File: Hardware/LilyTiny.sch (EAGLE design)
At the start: 13 parts, among them U1 ATTINY85

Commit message: Moved components to 0603 package size
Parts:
- C1: device SparkFun:CAP0402-CAP -> SparkFun:CAP0603-CAP
- R1: device SparkFun:RESISTOR0402-RES -> SparkFun:RESISTOR0603-RES
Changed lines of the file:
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@@
 <?xml version="1.0" encoding="utf-8"?>
 <!DOCTYPE eagle SYSTEM "eagle.dtd">
-<eagle version="6.1">
+<eagle version="6.4">
 <drawing>
 <settings>
@@
 <grid distance="0.1" unitdist="inch" unit="inch" style="lines" multiple="1" display="no" altdistance="0.01" altunitdist="inch" altunit="inch"/>
 <layers>
-<layer number="1" name="Top" color="4" fill="1" visible="no" active="no"/>
-<layer number="2" name="Route2" color="1" fill="3" visible="no" active="no"/>
-<layer number="3" name="Route3" color="4" fill="3" visible="no" active="no"/>
-<layer number="4" name="Route4" color="1" fill="4" visible="no" active="no"/>
-<layer number="5" name="Route5" color="4" fill="4" visible="no" active="no"/>
-<layer number="6" name="Route6" color="1" fill="8" visible="no" active="no"/>
-<layer number="7" name="Route7" color="4" fill="8" visible="no" active="no"/>
-<layer number="8" name="Route8" color="1" fill="2" visible="no" active="no"/>
-<layer number="9" name="Route9" color="4" fill="2" visible="no" active="no"/>
-<layer number="10" name="Route10" color="1" fill="7" visible="no" active="no"/>
-<layer number="11" name="Route11" color="4" fill="7" visible="no" active="no"/>
-<layer number="12" name="Route12" color="1" fill="5" visible="no" active="no"/>
-<layer number="13" name="Route13" color="4" fill="5" visible="no" active="no"/>
-<layer number="14" name="Route14" color="1" fill="6" visible="no" active="no"/>
-<layer number="15" name="Route15" color="4" fill="6" visible="no" active="no"/>
-<layer number="16" name="Bottom" color="1" fill="1" visible="no" active="no"/>
-<layer number="17" name="Pads" color="2" fill="1" visible="no" active="no"/>
-<layer number="18" name="Vias" color="2" fill="1" visible="no" active="no"/>
-<layer number="19" name="Unrouted" color="6" fill="1" visible="no" active="no"/>
-<layer number="20" name="Dimension" color="7" fill="1" visible="no" active="no"/>
-<layer number="21" name="tPlace" color="16" fill="1" visible="no" active="no"/>
-<layer number="22" name="bPlace" color="14" fill="1" visible="no" active="no"/>
-<layer number="23" name="tOrigins" color="15" fill="1" visible="no" active="no"/>
-<layer number="24" name="bOrigins" color="15" fill="1" visible="no" active="no"/>
-<layer number="25" name="tNames" color="7" fill="1" visible="no" active="no"/>
-<layer number="26" name="bNames" color="7" fill="1" visible="no" active="no"/>
-<layer number="27" name="tValues" color="7" fill="1" visible="no" active="no"/>
-<layer number="28" name="bValues" color="7" fill="1" visible="no" active="no"/>
+<layer number="1" name="Top" color="4" fill="1" visible="yes" active="no"/>
+<layer number="2" name="Route2" color="1" fill="3" visible="yes" active="no"/>
+<layer number="3" name="Route3" color="4" fill="3" visible="yes" active="no"/>
+<layer number="4" name="Route4" color="1" fill="4" visible="yes" active="no"/>
+<layer number="5" name="Route5" color="4" fill="4" visible="yes" active="no"/>
+<layer number="6" name="Route6" color="1" fill="8" visible="yes" active="no"/>
+<layer number="7" name="Route7" color="4" fill="8" visible="yes" active="no"/>
+<layer number="8" name="Route8" color="1" fill="2" visible="yes" active="no"/>
+<layer number="9" name="Route9" color="4" fill="2" visible="yes" active="no"/>
+<layer number="10" name="Route10" color="1" fill="7" visible="yes" active="no"/>
+<layer number="11" name="Route11" color="4" fill="7" visible="yes" active="no"/>
+<layer number="12" name="Route12" color="1" fill="5" visible="yes" active="no"/>
+<layer number="13" name="Route13" color="4" fill="5" visible="yes" active="no"/>
+<layer number="14" name="Route14" color="1" fill="6" visible="yes" active="no"/>
+<layer number="15" name="Route15" color="4" fill="6" visible="yes" active="no"/>
+<layer number="16" name="Bottom" color="1" fill="1" visible="yes" active="no"/>
+<layer number="17" name="Pads" color="2" fill="1" visible="yes" active="no"/>
+<layer number="18" name="Vias" color="2" fill="1" visible="yes" active="no"/>
+<layer number="19" name="Unrouted" color="6" fill="1" visible="yes" active="no"/>
+<layer number="20" name="Dimension" color="6" fill="1" visible="yes" active="no"/>
+<layer number="21" name="tPlace" color="16" fill="1" visible="yes" active="no"/>
+<layer number="22" name="bPlace" color="14" fill="1" visible="yes" active="no"/>
+<layer number="23" name="tOrigins" color="15" fill="1" visible="yes" active="no"/>
+<layer number="24" name="bOrigins" color="15" fill="1" visible="yes" active="no"/>
+<layer number="25" name="tNames" color="7" fill="1" visible="yes" active="no"/>
+<layer number="26" name="bNames" color="7" fill="1" visible="yes" active="no"/>
+<layer number="27" name="tValues" color="7" fill="1" visible="yes" active="no"/>
+<layer number="28" name="bValues" color="7" fill="1" visible="yes" active="no"/>
 <layer number="29" name="tStop" color="7" fill="3" visible="no" active="no"/>
 <layer number="30" name="bStop" color="7" fill="6" visible="no" active="no"/>
-<layer number="31" name="tCream" color="11" fill="4" visible="no" active="no"/>
+<layer number="31" name="tCream" color="7" fill="4" visible="no" active="no"/>
 <layer number="32" name="bCream" color="7" fill="5" visible="no" active="no"/>
 <layer number="33" name="tFinish" color="6" fill="3" visible="no" active="no"/>
@@
 <layer number="35" name="tGlue" color="7" fill="4" visible="no" active="no"/>
 <layer number="36" name="bGlue" color="7" fill="5" visible="no" active="no"/>
-<layer number="37" name="tTest" color="7" fill="1" visible="no" active="no"/>
-<layer number="38" name="bTest" color="7" fill="1" visible="no" active="no"/>
+<layer number="37" name="tTest" color="7" fill="1" visible="yes" active="no"/>
+<layer number="38" name="bTest" color="7" fill="1" visible="yes" active="no"/>
 <layer number="39" name="tKeepout" color="4" fill="11" visible="no" active="no"/>
 <layer number="40" name="bKeepout" color="1" fill="11" visible="no" active="no"/>
@@
 <layer number="44" name="Drills" color="7" fill="1" visible="no" active="no"/>
 <layer number="45" name="Holes" color="7" fill="1" visible="no" active="no"/>
-<layer number="46" name="Milling" color="3" fill="1" visible="no" active="no"/>
-<layer number="47" name="Measures" color="7" fill="1" visible="no" active="no"/>
-<layer number="48" name="Document" color="7" fill="1" visible="no" active="no"/>
-<layer number="49" name="Reference" color="13" fill="1" visible="no" active="no"/>
-<layer number="50" name="dxf" color="7" fill="1" visible="no" active="no"/>
-<layer number="51" name="tDocu" color="14" fill="1" visible="no" active="no"/>
-<layer number="52" name="bDocu" color="7" fill="1" visible="no" active="no"/>
-<layer number="53" name="tGND_GNDA" color="7" fill="9" visible="no" active="no"/>
-<layer number="54" name="bGND_GNDA" color="1" fill="9" visible="no" active="no"/>
-<layer number="56" name="wert" color="7" fill="1" visible="no" active="no"/>
+<layer number="46" name="Milling" color="3" fill="1" visible="yes" active="no"/>
+<layer number="47" name="Measures" color="7" fill="1" visible="yes" active="no"/>
+<layer number="48" name="Document" color="7" fill="1" visible="yes" active="no"/>
+<layer number="49" name="Reference" color="7" fill="1" visible="yes" active="no"/>
+<layer number="50" name="dxf" color="7" fill="1" visible="yes" active="no"/>
+<layer number="51" name="tDocu" color="6" fill="1" visible="yes" active="no"/>
+<layer number="52" name="bDocu" color="7" fill="1" visible="yes" active="no"/>
+<layer number="53" name="tGND_GNDA" color="7" fill="9" visible="yes" active="no"/>
+<layer number="54" name="bGND_GNDA" color="1" fill="9" visible="yes" active="no"/>
+<layer number="56" name="wert" color="7" fill="1" visible="yes" active="no"/>
 <layer number="91" name="Nets" color="2" fill="1" visible="yes" active="yes"/>
 <layer number="92" name="Busses" color="1" fill="1" visible="yes" active="yes"/>
@@
 <part name="FRAME1" library="SparkFun" deviceset="FRAME-LETTER" device=""/>
 <part name="U1" library="SparkFun" deviceset="ATTINY45" device="" value="ATTINY85"/>
-<part name="C1" library="SparkFun" deviceset="CAP" device="0402-CAP" value="0.1uF"/>
-<part name="R1" library="SparkFun" deviceset="RESISTOR" device="0402-RES" value="10k"/>
+<part name="C1" library="SparkFun" deviceset="CAP" device="0603-CAP" value="0.1uF"/>
+<part name="R1" library="SparkFun" deviceset="RESISTOR" device="0603-RES" value="10k"/>
 <part name="GND1" library="SparkFun" deviceset="GND" device=""/>
 <part name="P+1" library="SparkFun" deviceset="VCC" device=""/>

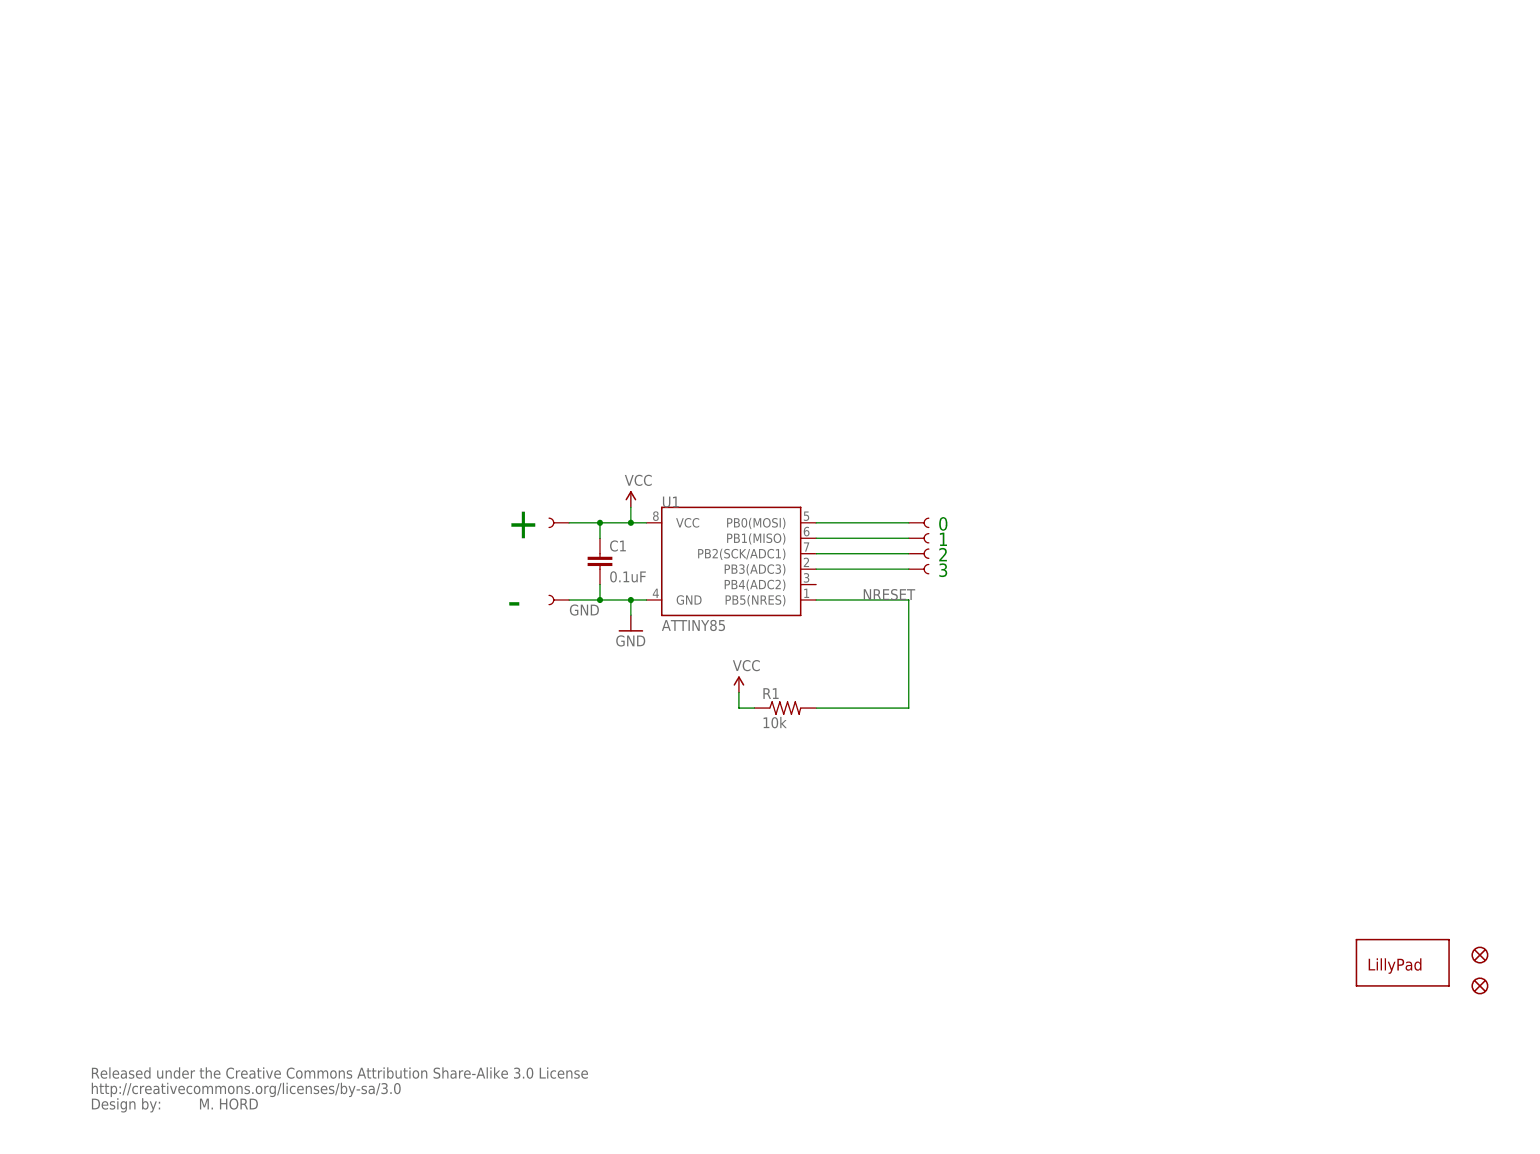
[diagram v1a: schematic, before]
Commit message: Moved to 0603 components, added OSHW logo
-moved R1 and C1 a bit to fit in 0603 packages. Had to re-route some
traces.
-Added OSHW.
-Updated Frame.
-added version to both sch and brd
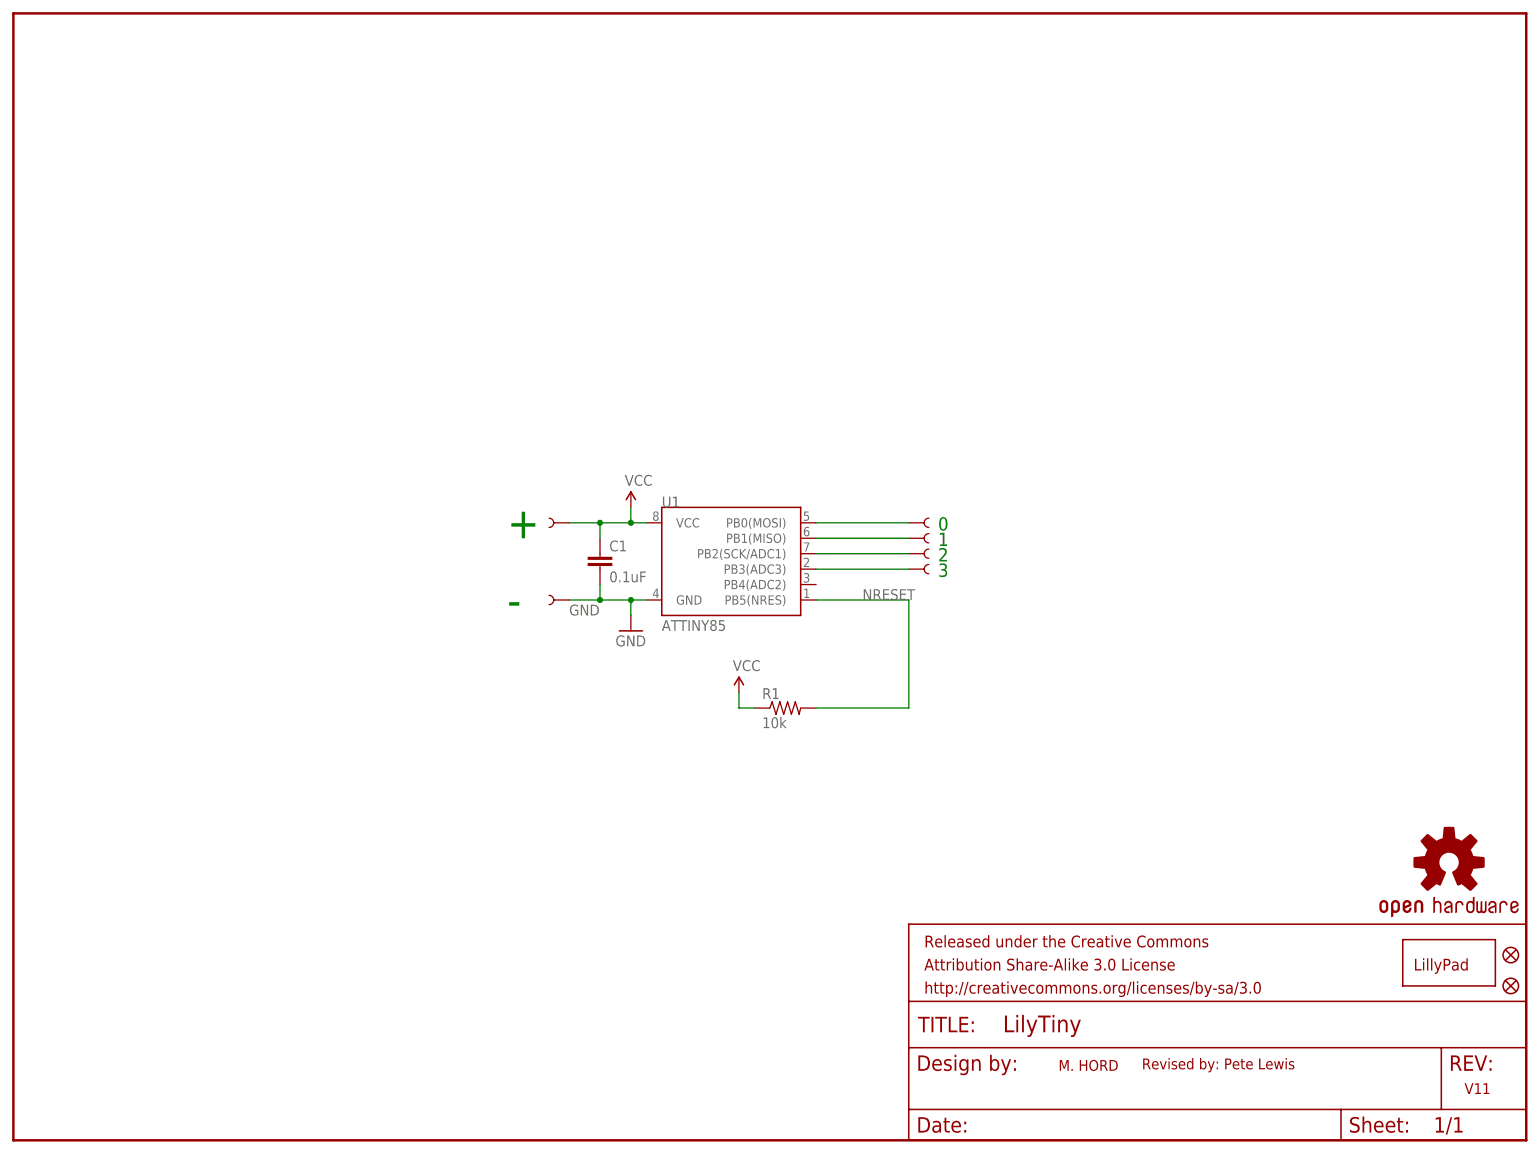
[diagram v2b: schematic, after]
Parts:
- removed U$1: CREATIVE_COMMONS, SparkFun:CREATIVE_COMMONS
- added FRAME2: FRAME-LETTER, SparkFun-Aesthetics:FRAME-LETTER
- added LOGO1: OSHW-LOGOS, SparkFun-Aesthetics:OSHW-LOGOS
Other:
- note added: "Revised by: Pete Lewis"
- note added: "V11"
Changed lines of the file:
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@@
 <layer number="144" name="Drill_legend" color="7" fill="1" visible="yes" active="yes"/>
 <layer number="151" name="HeatSink" color="7" fill="1" visible="yes" active="yes"/>
+<layer number="199" name="Contour" color="7" fill="1" visible="no" active="yes"/>
 <layer number="200" name="200bmp" color="1" fill="10" visible="yes" active="yes"/>
 <layer number="201" name="201bmp" color="2" fill="10" visible="yes" active="yes"/>
@@
 </classes>
 <parts>
-<part name="FRAME1" library="SparkFun" deviceset="FRAME-LETTER" device=""/>
 <part name="U1" library="SparkFun" deviceset="ATTINY45" device="" value="ATTINY85"/>
 <part name="C1" library="SparkFun" deviceset="CAP" device="0603-CAP" value="0.1uF"/>
@@
 <part name="U$7" library="LilyPad-Wearables" deviceset="SEWTAP" device="6"/>
 <part name="P+2" library="SparkFun" deviceset="VCC" device=""/>
-<part name="U$1" library="SparkFun" deviceset="CREATIVE_COMMONS" device=""/>
 <part name="U$8" library="LilyPad-Wearables" deviceset="LOGO-LP" device="L"/>
 <part name="JP1" library="SparkFun" deviceset="FIDUCIAL" device="UFIDUCIAL"/>
 <part name="JP2" library="SparkFun" deviceset="FIDUCIAL" device="UFIDUCIAL"/>
+<part name="FRAME2" library="SparkFun-Aesthetics" deviceset="FRAME-LETTER" device=""/>
+<part name="LOGO1" library="SparkFun-Aesthetics" deviceset="OSHW-LOGO" device="S"/>
 </parts>
 <sheets>
 <sheet>
 <plain>
-<text x="-88.9" y="-88.9" size="1.778" layer="95">M. HORD</text>
+<text x="52.578" y="-82.55" size="1.778" layer="94">M. HORD</text>
 <text x="-38.1" y="5.08" size="5.08" layer="91">+</text>
 <text x="-38.1" y="-7.62" size="5.08" layer="91">-</text>
@@
 <text x="32.766" y="1.27" size="2.1844" layer="91">2</text>
 <text x="32.766" y="-1.27" size="2.1844" layer="91">3</text>
+<text x="66.294" y="-82.296" size="1.778" layer="94">Revised by: Pete Lewis</text>
+<text x="119.38" y="-86.36" size="1.778" layer="94">V11</text>
 </plain>
 <instances>
-<instance part="FRAME1" gate="G$1" x="-119.38" y="-93.98"/>
-<instance part="FRAME1" gate="G$2" x="27.94" y="-93.98"/>
 <instance part="U1" gate="G$1" x="0" y="0"/>
 <instance part="C1" gate="G$1" x="-22.86" y="0"/>
@@
 <instance part="U$7" gate="G$1" x="30.48" y="7.62"/>
 <instance part="P+2" gate="1" x="0" y="-20.32"/>
-<instance part="U$1" gate="G$1" x="-106.68" y="-88.9"/>
-<instance part="U$8" gate="G$1" x="104.14" y="-66.04"/>
-<instance part="JP1" gate="G$1" x="121.92" y="-63.5"/>
-<instance part="JP2" gate="G$1" x="121.92" y="-68.58"/>
+<instance part="U$8" gate="G$1" x="111.76" y="-66.04"/>
+<instance part="JP1" gate="G$1" x="127" y="-63.5"/>
+<instance part="JP2" gate="G$1" x="127" y="-68.58"/>
+<instance part="FRAME2" gate="G$1" x="-119.38" y="-93.98"/>
+<instance part="FRAME2" gate="G$2" x="27.94" y="-93.98"/>
+<instance part="LOGO1" gate="G$1" x="116.84" y="-48.26"/>
 </instances>
 <busses>
